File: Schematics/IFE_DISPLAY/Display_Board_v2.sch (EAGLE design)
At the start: 79 parts, among them Q1 16MHz, Q3 16MHz, U4 HEX_CONVERTER, U5 HEX_CONVERTER

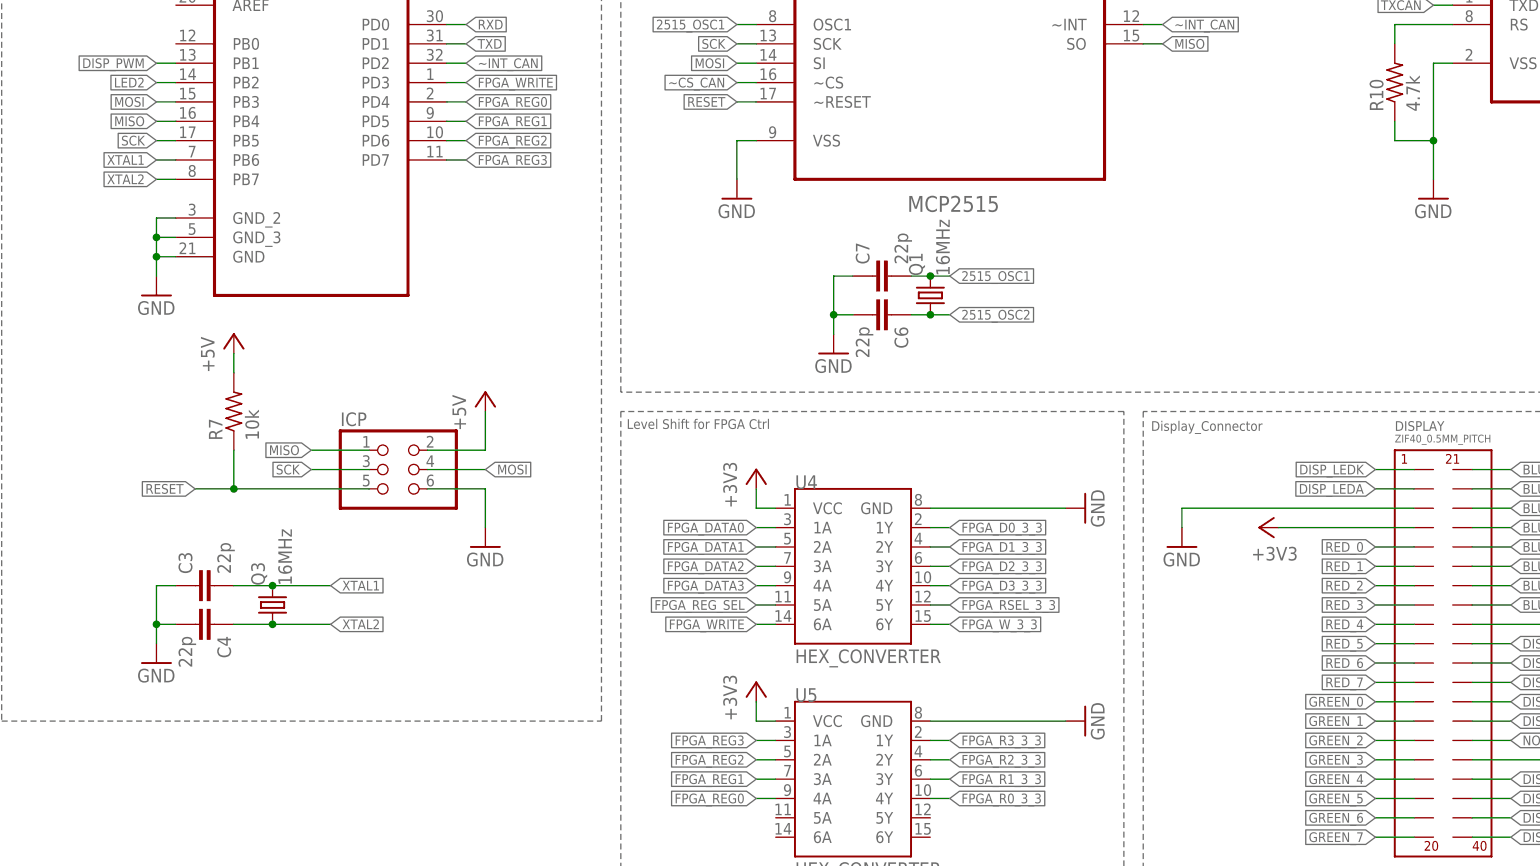
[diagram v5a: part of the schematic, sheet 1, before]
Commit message: Updted Oscillators, routing ~60%
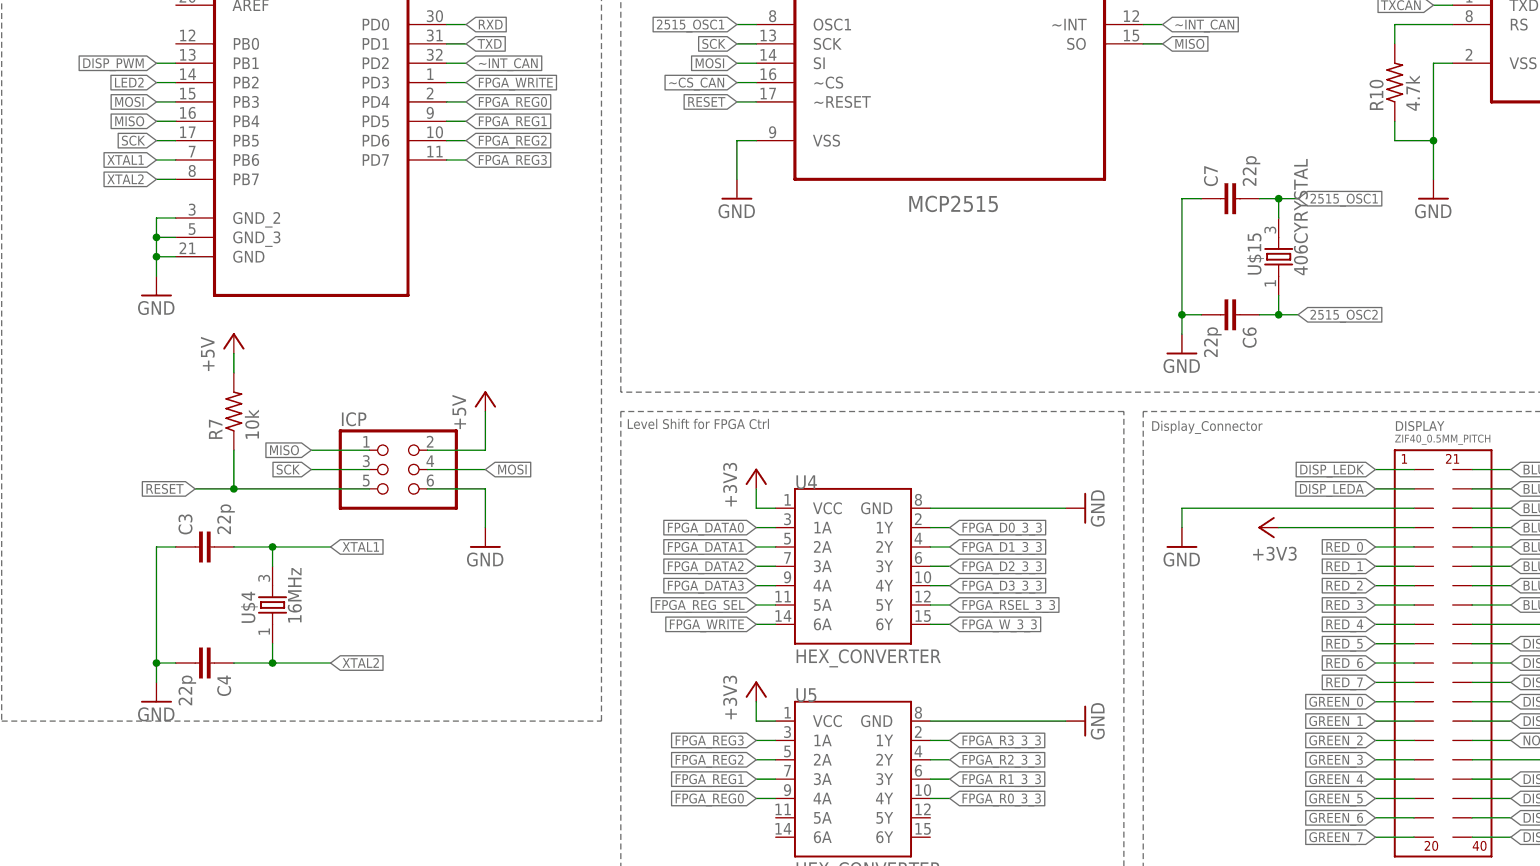
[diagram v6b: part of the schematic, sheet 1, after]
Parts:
- removed 50MHZ: SM77H, crystal:SM77H
- removed Q1, Q3: 16MHz, adafruit:CRYSTALCTS406
- added U$1: SM77H, Display_Custom:SM77H
- added U$15: 406CYRYSTAL, Display_Custom:406CYRYSTAL
- added U$4: 16MHz, Display_Custom:406CYRYSTAL
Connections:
- net +3V3: now also U$1.VCC; no longer 50MHZ.VCC
- net 2515_OSC1: now also U$15.2; no longer Q1.2
- net 2515_OSC2: now also U$15.1; no longer Q1.1
- net 50_MHZ: now also U$1.OUT; no longer 50MHZ.OUT
- net GND: now also U$1.GND; no longer 50MHZ.GND
- net XTAL1: now also U$4.2; no longer Q3.2
- net XTAL2: now also U$4.1; no longer Q3.1
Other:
- moved on the sheet: C3, C4, C6, C7
